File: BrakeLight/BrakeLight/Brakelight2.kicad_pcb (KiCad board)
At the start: 2 copper layers, 103.6 x 28.3 mm, 41 parts, among them J1 Conn_01x02

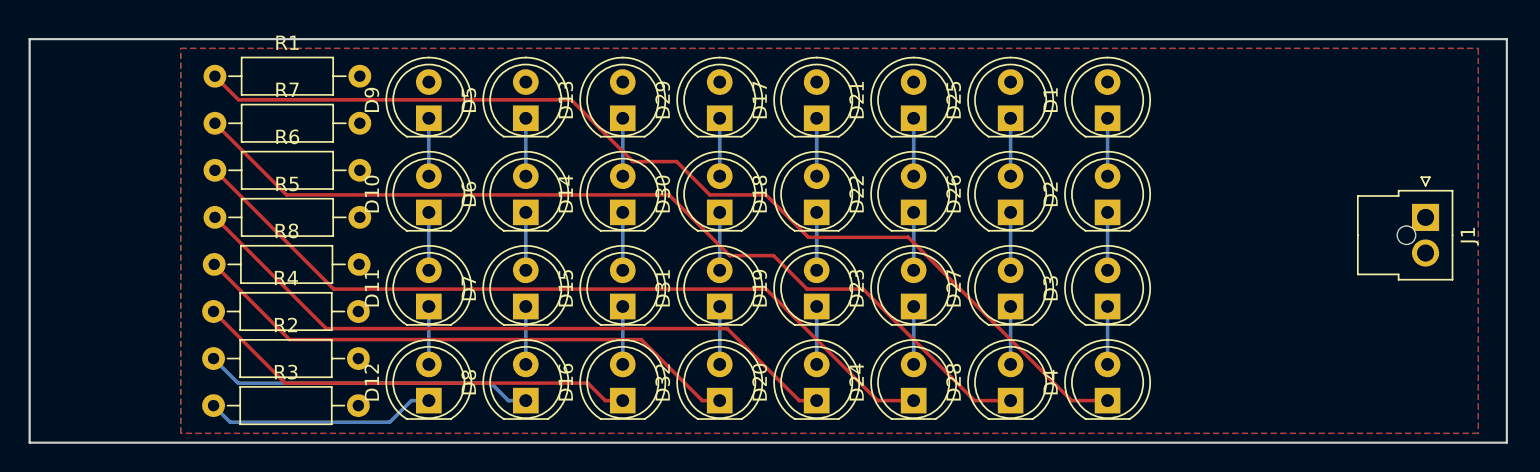
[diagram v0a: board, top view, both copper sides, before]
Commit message: Need to correct Bay Area DFM warnings on TSAL. Brake Light passed and ready to be sent.
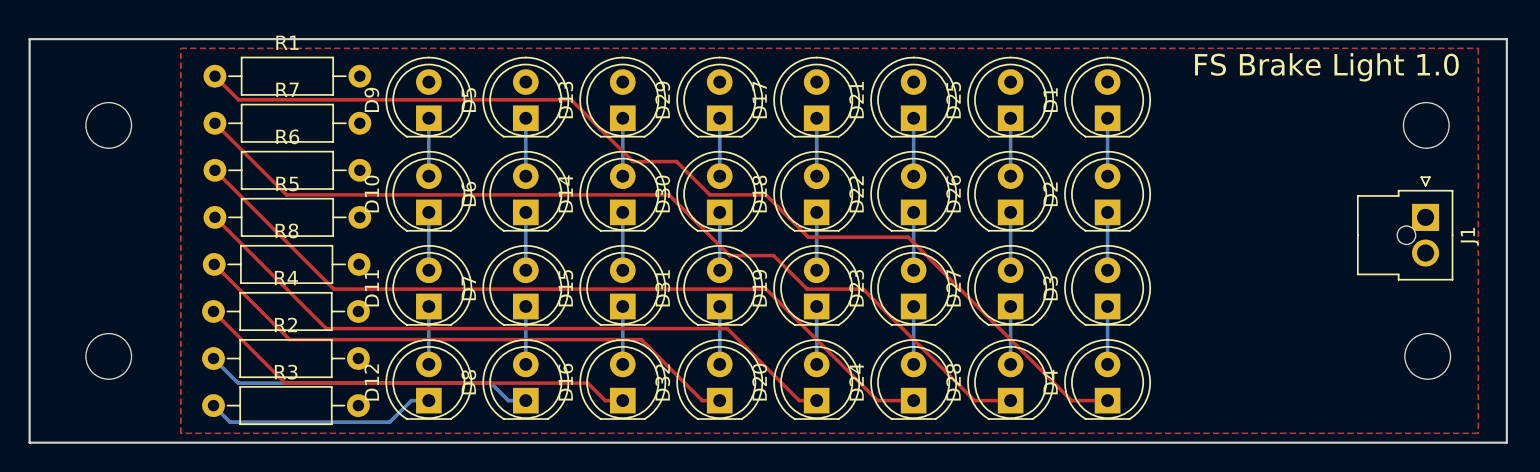
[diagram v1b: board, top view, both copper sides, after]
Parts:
- added J2: Conn_01x01, Mounting_Holes:MountingHole_3.2mm_M3, F.Cu at (87.0, 49.1)
- added J3: Conn_01x01, Mounting_Holes:MountingHole_3.2mm_M3, F.Cu at (87.0, 33.0)
- added J4: Conn_01x01, Mounting_Holes:MountingHole_3.2mm_M3, F.Cu at (179.4, 33.0)
- added J5: Conn_01x01, Mounting_Holes:MountingHole_3.2mm_M3, F.Cu at (179.5, 49.1)
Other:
- net class Default: via_dia 0.6 -> 0.8
- board text added: "FS Brake Light 1.0"
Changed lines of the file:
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@@
     (links 48)
     (no_connects 0)
-    (area 0 0 0 0)
+    (area 81.339519 18.741992 210.438267 66.45572)
     (thickness 1.6)
-    (drawings 13)
+    (drawings 12)
     (tracks 66)
     (zones 0)
-    (modules 41)
-    (nets 35)
+    (modules 45)
+    (nets 39)
   )
   (page A4)
@@
     (38 B.Mask user)
     (39 F.Mask user)
-    (40 Dwgs.User user hide)
-    (41 Cmts.User user)
+    (40 Dwgs.User user)
+    (41 Cmts.User user hide)
     (42 Eco1.User user)
     (43 Eco2.User user)
@@
     (segment_width 0.2)
     (edge_width 0.15)
-    (via_size 0.6)
+    (via_size 0.8)
     (via_drill 0.4)
     (via_min_size 0.4)
@@
     (aux_axis_origin 0 0)
     (grid_origin 0.05 0.05)
-    (visible_elements FFFCFF7F)
+    (visible_elements 7FFFFFFF)
     (pcbplotparams
-      (layerselection 0x00030_80000001)
+      (layerselection 0x010fc_80000001)
       (usegerberextensions false)
       (excludeedgelayer true)
@@
       (outputformat 1)
       (mirror false)
-      (drillshape 1)
+      (drillshape 0)
       (scaleselection 1)
-      (outputdirectory ""))
+      (outputdirectory BrakeLightBayAreaPrep/))
   )
   (net 0 "")
@@
   (net 33 "Net-(D7-Pad1)")
   (net 34 "Net-(D8-Pad1)")
+  (net 35 "Net-(J2-Pad1)")
+  (net 36 "Net-(J3-Pad1)")
+  (net 37 "Net-(J4-Pad1)")
+  (net 38 "Net-(J5-Pad1)")
   (net_class Default "This is the default net class."
     (clearance 0.2)
     (trace_width 0.25)
-    (via_dia 0.6)
+    (via_dia 0.8)
     (via_drill 0.4)
     (uvia_dia 0.3)
@@
     (add_net "Net-(D7-Pad1)")
     (add_net "Net-(D8-Pad1)")
+    (add_net "Net-(J2-Pad1)")
+    (add_net "Net-(J3-Pad1)")
+    (add_net "Net-(J4-Pad1)")
+    (add_net "Net-(J5-Pad1)")
   )
   (module LEDs:LED_D5.0mm (layer F.Cu)
@@
     )
   )
+  (module Mounting_Holes:MountingHole_3.2mm_M3 (layer F.Cu)
+    (at 87 49.15)
+    (descr "Mounting Hole 3.2mm, no annular, M3")
+    (tags "mounting hole 3.2mm no annular m3")
+    (attr virtual)
+    (fp_text reference J2 (at 0 -4.2) (layer F.SilkS) hide
+      (effects (font (size 1 1) (thickness 0.15)))
+    )
+    (fp_text value Conn_01x01 (at 0 4.2) (layer F.Fab)
+      (effects (font (size 1 1) (thickness 0.15)))
+    )
+    (fp_text user %R (at 0.3 0) (layer F.Fab)
+      (effects (font (size 1 1) (thickness 0.15)))
+    )
+    (fp_circle (center 0 0) (end 3.2 0) (layer Cmts.User) (width 0.15))
+    (fp_circle (center 0 0) (end 3.45 0) (layer F.CrtYd) (width 0.05))
+    (pad 1 np_thru_hole circle (at 0 0) (size 3.2 3.2) (drill 3.2) (layers *.Cu *.Mask)
+      (net 35 "Net-(J2-Pad1)"))
+  )
+  (module Mounting_Holes:MountingHole_3.2mm_M3 (layer F.Cu)
+    (at 87 32.95)
+    (descr "Mounting Hole 3.2mm, no annular, M3")
+    (tags "mounting hole 3.2mm no annular m3")
+    (attr virtual)
+    (fp_text reference J3 (at 0 -4.2) (layer F.SilkS) hide
+      (effects (font (size 1 1) (thickness 0.15)))
+    )
+    (fp_text value Conn_01x01 (at 0 4.2) (layer F.Fab)
+      (effects (font (size 1 1) (thickness 0.15)))
+    )
+    (fp_text user %R (at 0.3 0) (layer F.Fab)
+      (effects (font (size 1 1) (thickness 0.15)))
+    )
+    (fp_circle (center 0 0) (end 3.2 0) (layer Cmts.User) (width 0.15))
+    (fp_circle (center 0 0) (end 3.45 0) (layer F.CrtYd) (width 0.05))
+    (pad 1 np_thru_hole circle (at 0 0) (size 3.2 3.2) (drill 3.2) (layers *.Cu *.Mask)
+      (net 36 "Net-(J3-Pad1)"))
+  )
+  (module Mounting_Holes:MountingHole_3.2mm_M3 (layer F.Cu)
+    (at 179.4 32.95)
+    (descr "Mounting Hole 3.2mm, no annular, M3")
+    (tags "mounting hole 3.2mm no annular m3")
+    (attr virtual)
+    (fp_text reference J4 (at 2.2 -2.15) (layer F.SilkS) hide
+      (effects (font (size 1 1) (thickness 0.15)))
+    )
+    (fp_text value Conn_01x01 (at 0 4.2) (layer F.Fab)
+      (effects (font (size 1 1) (thickness 0.15)))
+    )
+    (fp_text user %R (at 0.3 0) (layer F.Fab)
+      (effects (font (size 1 1) (thickness 0.15)))
+    )
+    (fp_circle (center 0 0) (end 3.2 0) (layer Cmts.User) (width 0.15))
+    (fp_circle (center 0 0) (end 3.45 0) (layer F.CrtYd) (width 0.05))
+    (pad 1 np_thru_hole circle (at 0 0) (size 3.2 3.2) (drill 3.2) (layers *.Cu *.Mask)
+      (net 37 "Net-(J4-Pad1)"))
+  )
+  (module Mounting_Holes:MountingHole_3.2mm_M3 (layer F.Cu)
+    (at 179.5 49.15)
+    (descr "Mounting Hole 3.2mm, no annular, M3")
+    (tags "mounting hole 3.2mm no annular m3")
+    (attr virtual)
+    (fp_text reference J5 (at 0 -4.2) (layer F.SilkS) hide
+      (effects (font (size 1 1) (thickness 0.15)))
+    )
+    (fp_text value Conn_01x01 (at 0 4.2) (layer F.Fab)
+      (effects (font (size 1 1) (thickness 0.15)))
+    )
+    (fp_text user %R (at 0.3 0) (layer F.Fab)
+      (effects (font (size 1 1) (thickness 0.15)))
+    )
+    (fp_circle (center 0 0) (end 3.2 0) (layer Cmts.User) (width 0.15))
+    (fp_circle (center 0 0) (end 3.45 0) (layer F.CrtYd) (width 0.05))
+    (pad 1 np_thru_hole circle (at 0 0) (size 3.2 3.2) (drill 3.2) (layers *.Cu *.Mask)
+      (net 38 "Net-(J5-Pad1)"))
+  )
+  (dimension 103.750193 (width 0.3) (layer Cmts.User)
+    (gr_text "103.750 mm" (at 133.217121 65.005721 359.8895504) (layer Cmts.User)
+      (effects (font (size 1.5 1.5) (thickness 0.3)))
+    )
+    (feature1 (pts (xy 81.375 47.85) (xy 81.339519 66.255719)))
+    (feature2 (pts (xy 185.125 48.05) (xy 185.089519 66.455719)))
+    (crossbar (pts (xy 185.094724 63.755724) (xy 81.344724 63.555724)))
+    (arrow1a (pts (xy 81.344724 63.555724) (xy 82.472356 62.971476)))
+    (arrow1b (pts (xy 81.344724 63.555724) (xy 82.470095 64.144315)))
+    (arrow2a (pts (xy 185.094724 63.755724) (xy 183.969353 63.167133)))
+    (arrow2b (pts (xy 185.094724 63.755724) (xy 183.967092 64.339972)))
+  )
+  (dimension 28.450011 (width 0.3) (layer Cmts.User)
+    (gr_text "28.450 mm" (at 203.938267 41.076011 89.94965223) (layer Cmts.User)
+      (effects (font (size 1.5 1.5) (thickness 0.3)))
+    )
+    (feature1 (pts (xy 174.35 26.825) (xy 205.300767 26.852198)))
+    (feature2 (pts (xy 174.325 55.275) (xy 205.275767 55.302198)))
+    (crossbar (pts (xy 202.575768 55.299825) (xy 202.600768 26.849825)))
+    (arrow1a (pts (xy 202.600768 26.849825) (xy 203.186199 27.976844)))
+    (arrow1b (pts (xy 202.600768 26.849825) (xy 202.013358 27.975813)))
+    (arrow2a (pts (xy 202.575768 55.299825) (xy 203.163178 54.173837)))
+    (arrow2b (pts (xy 202.575768 55.299825) (xy 201.990337 54.172806)))
+  )
+  (gr_text "FS Brake Light 1.0" (at 172.4 28.75) (layer F.SilkS)
+    (effects (font (size 1.5 1.5) (thickness 0.3)))
+  )
   (gr_line (start 185.05 26.9) (end 81.45 26.9) (angle 90) (layer Edge.Cuts) (width 0.15))
   (gr_line (start 185.05 55.2) (end 185.05 26.9) (angle 90) (layer Edge.Cuts) (width 0.15))
@@
     (arrow2b (pts (xy 106.2 59.95) (xy 105.073496 60.536421)))
   )
-  (gr_circle (center 178 50.1) (end 174.8 49.85) (layer Cmts.User) (width 0.2))
-  (gr_circle (center 178.5 31.45) (end 175.3 31.3) (layer Cmts.User) (width 0.2))
-  (gr_circle (center 87.15 49.3) (end 83.95 49.6) (layer Cmts.User) (width 0.2))
-  (gr_circle (center 87.45 32.65) (end 84.25 32.55) (layer Cmts.User) (width 0.2))
   (dimension 12.800098 (width 0.3) (layer Dwgs.User)
     (gr_text "12.800 mm" (at 166.663085 20.724939 0.2238105004) (layer Dwgs.User)
